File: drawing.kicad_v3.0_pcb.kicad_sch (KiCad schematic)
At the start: 39 parts, among them IC1 DW01A-G, J1 Micro USB Chargeport, J2 Prog headers, J3 128x32 I2C OLED, J4 TP4056, J5 MK-12C02, J6 Conn_01x02, Q1 FS8205, U1 HT7333-SOT89, U2 ESP-12E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

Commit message: Updated charging circuit
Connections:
- net Batt+: now also J6.2 (Pin_2); no longer J6.1 (Pin_1)
- net GND: now also C4.2, IC1.6 (GND), J6.1 (Pin_1), Q1.1 (S1), Q1.3 (S2); no longer J1.4 (ID), Q1.2 (D12_1)
- net at R12.1: now also J4.6 (~{STDBY}); no longer J4.7 (~{CHRG})
- net at IC1.5 (VCC), R14.2: now also C4.1; no longer C4.2
- net at R10.2: now also J4.7 (~{CHRG}); no longer J4.6 (~{STDBY})
- net +5V: no longer names the net of C2.2, D5.2 (A), D6.2 (A), J1.1 (VBUS), J4.4 (VCC4), J4.8 (CE)
- removed net Batt-: C4.1, IC1.6 (GND), J6.2 (Pin_2), Q1.5 (D12_2)
- no-connect marks 19 -> 22
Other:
- moved on the sheet: C1, C2, C3, D5, D6, D7, J1, J2, J3, J4, J5, J6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

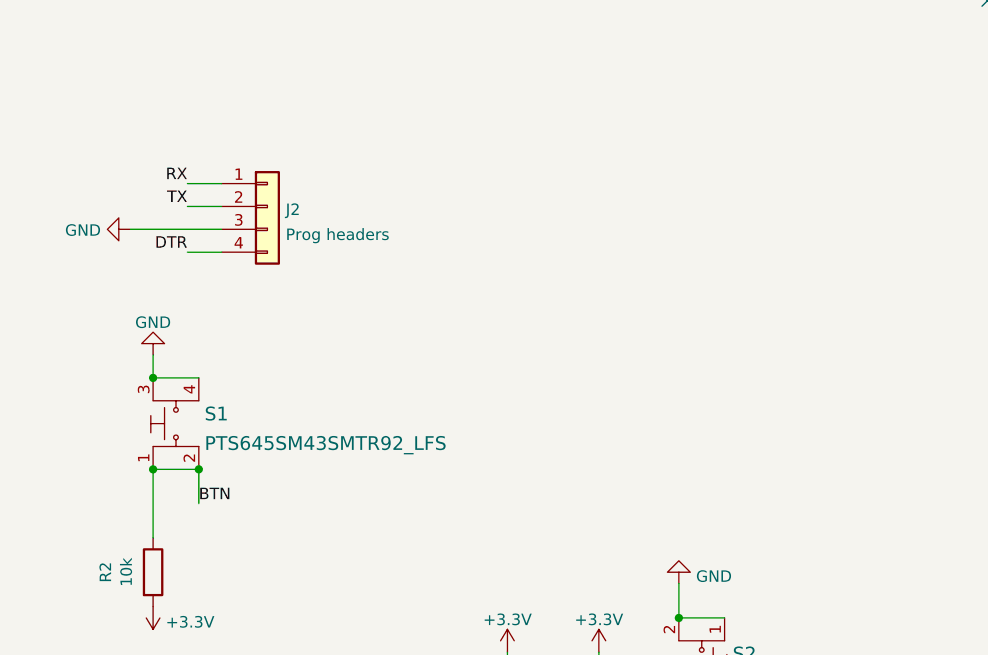
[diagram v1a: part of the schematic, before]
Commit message: Fixed charging circuit in v3.0
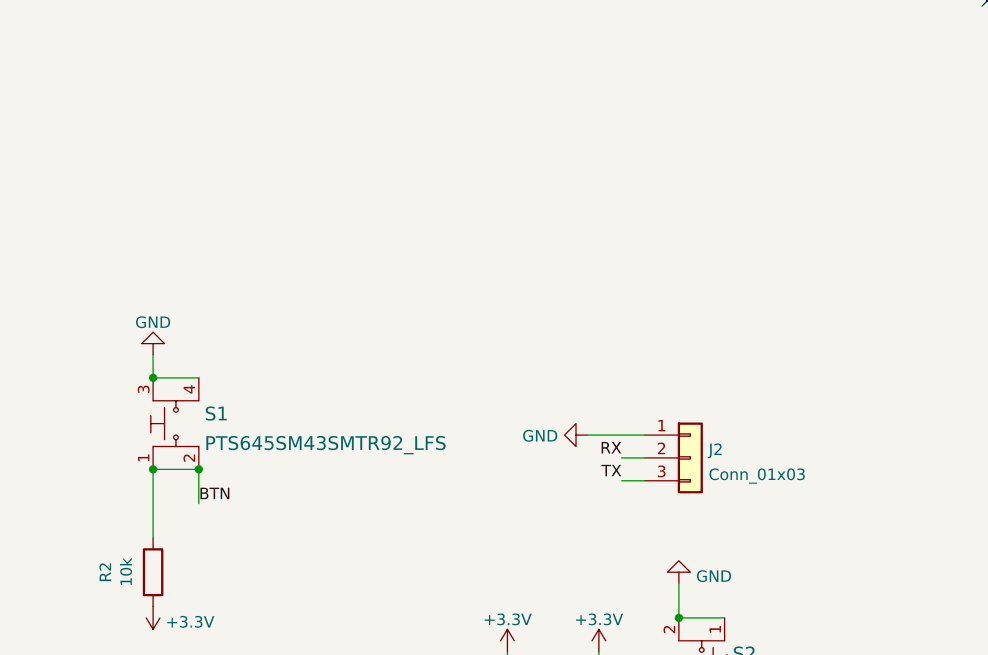
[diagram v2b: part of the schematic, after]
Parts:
- removed J2: Prog headers, Connector_PinSocket_2.54mm:PinSocket_1x04_P2.54mm_Horizontal, symbol Connector_Generic:Conn_01x04
- added J2: Conn_01x03, Connector_PinSocket_2.54mm:PinSocket_1x03_P2.54mm_Horizontal, symbol Connector_Generic:Conn_01x03
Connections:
- net GND: now also J2.1 (Pin_1)
- net RX: now also J2.2 (Pin_2)
- net TX: now also J2.3 (Pin_3)
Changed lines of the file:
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@@
-    (stroke (width 0) (type default) (color 0 0 0 0))
-  )
-  (wire (pts (xy 30.48 82.55) (xy 34.29 82.55))
     (stroke (width 0) (type default) (color 0 0 0 0))
   )
@@
     (stroke (width 0) (type default) (color 0 0 0 0))
   )
-  (wire (pts (xy 24.13 85.09) (xy 34.29 85.09))
-    (stroke (width 0) (type default) (color 0 0 0 0))
-  )
   (wire (pts (xy 231.14 24.13) (xy 238.76 24.13))
     (stroke (width 0) (type default) (color 0 0 0 0))
@@
     (stroke (width 0) (type default) (color 0 0 0 0))
   )
+  (wire (pts (xy 74.93 107.95) (xy 81.28 107.95))
+    (stroke (width 0) (type default) (color 0 0 0 0))
+  )
   (wire (pts (xy 102.87 182.88) (xy 97.79 182.88))
     (stroke (width 0) (type default) (color 0 0 0 0))
@@
     (stroke (width 0) (type default) (color 0 0 0 0))
   )
+  (wire (pts (xy 78.74 113.03) (xy 81.28 113.03))
+    (stroke (width 0) (type default) (color 0 0 0 0))
+  )
   (wire (pts (xy 113.03 160.02) (xy 116.84 160.02))
     (stroke (width 0) (type default) (color 0 0 0 0))
@@
     (stroke (width 0) (type default) (color 0 0 0 0))
   )
-  (wire (pts (xy 30.48 80.01) (xy 34.29 80.01))
-    (stroke (width 0) (type default) (color 0 0 0 0))
-  )
   (wire (pts (xy 130.81 172.72) (xy 130.81 189.23))
     (stroke (width 0) (type default) (color 0 0 0 0))
@@
     (stroke (width 0) (type default) (color 0 0 0 0))
   )
+  (wire (pts (xy 78.74 110.49) (xy 81.28 110.49))
+    (stroke (width 0) (type default) (color 0 0 0 0))
+  )
   (wire (pts (xy 204.47 24.13) (xy 205.74 24.13))
     (stroke (width 0) (type default) (color 0 0 0 0))
@@
   )
   (wire (pts (xy 116.84 186.69) (xy 121.92 186.69))
-    (stroke (width 0) (type default) (color 0 0 0 0))
-  )
-  (wire (pts (xy 30.48 87.63) (xy 34.29 87.63))
     (stroke (width 0) (type default) (color 0 0 0 0))
   )
@@
     (effects (font (size 1.27 1.27)) (justify right bottom))
   )
+  (label "TX" (at 78.74 113.03 180)
+    (effects (font (size 1.27 1.27)) (justify right bottom))
+  )
   (label "SCL" (at 34.29 144.78 0)
     (effects (font (size 1.27 1.27)) (justify left bottom))
@@
     (effects (font (size 1.27 1.27)) (justify right bottom))
   )
-  (label "TX" (at 30.48 82.55 180)
-    (effects (font (size 1.27 1.27)) (justify right bottom))
-  )
   (label "SDA" (at 116.84 160.02 0)
     (effects (font (size 1.27 1.27)) (justify left bottom))
@@
     (effects (font (size 1.27 1.27)) (justify left bottom))
   )
-  (label "RX" (at 30.48 80.01 180)
-    (effects (font (size 1.27 1.27)) (justify right bottom))
-  )
   (label "LC" (at 35.56 46.99 270)
     (effects (font (size 1.27 1.27)) (justify right bottom))
@@
     (effects (font (size 1.27 1.27)) (justify left bottom))
   )
-  (label "DTR" (at 30.48 87.63 180)
+  (label "RX" (at 78.74 110.49 180)
     (effects (font (size 1.27 1.27)) (justify right bottom))
   )
@@
     (pin "1")
   )
+  (symbol (lib_id "power:GND") (at 74.93 107.95 270) (unit 1)
+    (in_bom yes) (on_board yes)
+    (property "Reference" "#PWR02" (id 0) (at 68.58 107.95 0)
+      (effects (font (size 1.27 1.27)) hide)
+    )
+    (property "Value" "GND" (id 1) (at 71.6788 108.077 90)
+      (effects (font (size 1.27 1.27)) (justify right))
+    )
+    (property "Footprint" "" (id 2) (at 74.93 107.95 0)
+      (effects (font (size 1.27 1.27)) hide)
+    )
+    (property "Datasheet" "" (id 3) (at 74.93 107.95 0)
+      (effects (font (size 1.27 1.27)) hide)
+    )
+    (pin "1")
+  )
   (symbol (lib_id "Connector_Generic:Conn_01x04") (at 24.13 147.32 180) (unit 1)
     (in_bom yes) (on_board yes) (fields_autoplaced)
@@
     (pin "1")
     (pin "2")
+  )
+  (symbol (lib_id "Connector_Generic:Conn_01x03") (at 86.36 110.49 0) (unit 1)
+    (in_bom yes) (on_board yes) (fields_autoplaced)
+    (property "Reference" "J2" (id 0) (at 88.392 109.5815 0)
+      (effects (font (size 1.27 1.27)) (justify left))
+    )
+    (property "Value" "Conn_01x03" (id 1) (at 88.392 112.3566 0)
+      (effects (font (size 1.27 1.27)) (justify left))
+    )
+    (property "Footprint" "Connector_PinSocket_2.54mm:PinSocket_1x03_P2.54mm_Horizontal" (id 2) (at 86.36 110.49 0)
+      (effects (font (size 1.27 1.27)) hide)
+    )
+    (property "Datasheet" "~" (id 3) (at 86.36 110.49 0)
+      (effects (font (size 1.27 1.27)) hide)
+    )
+    (pin "1")
+    (pin "2")
+    (pin "3")
   )
   (symbol (lib_id "Device:R") (at 130.81 149.86 270) (unit 1)
@@
     (property "Status" "Active" (id 12) (at 118.11 138.43 0)
       (effects (font (size 1.524 1.524)) (justify left) hide)
-    )
-    (pin "1")
-    (pin "2")
-    (pin "3")
-    (pin "4")
-  )
-  (symbol (lib_id "Connector_Generic:Conn_01x04") (at 39.37 82.55 0) (unit 1)
-    (in_bom yes) (on_board yes) (fields_autoplaced)
-    (property "Reference" "J2" (id 0) (at 41.402 82.9115 0)
-      (effects (font (size 1.27 1.27)) (justify left))
-    )
-    (property "Value" "Prog headers" (id 1) (at 41.402 85.6866 0)
-      (effects (font (size 1.27 1.27)) (justify left))
-    )
-    (property "Footprint" "Connector_PinSocket_2.54mm:PinSocket_1x04_P2.54mm_Horizontal" (id 2) (at 39.37 82.55 0)
-      (effects (font (size 1.27 1.27)) hide)
-    )
-    (property "Datasheet" "~" (id 3) (at 39.37 82.55 0)
-      (effects (font (size 1.27 1.27)) hide)
     )
     (pin "1")
@@
     (pin "2")
   )
-  (symbol (lib_id "power:GND") (at 24.13 85.09 270) (unit 1)
-    (in_bom yes) (on_board yes)
-    (property "Reference" "#PWR02" (id 0) (at 17.78 85.09 0)
-      (effects (font (size 1.27 1.27)) hide)
-    )
-    (property "Value" "GND" (id 1) (at 20.8788 85.217 90)
-      (effects (font (size 1.27 1.27)) (justify right))
-    )
-    (property "Footprint" "" (id 2) (at 24.13 85.09 0)
-      (effects (font (size 1.27 1.27)) hide)
-    )
-    (property "Datasheet" "" (id 3) (at 24.13 85.09 0)
-      (effects (font (size 1.27 1.27)) hide)
-    )
-    (pin "1")
-  )
   (symbol (lib_id "dk_Tactile-Switches:PTS645SM43SMTR92_LFS") (at 29.21 106.68 90) (unit 1)
     (in_bom yes) (on_board yes) (fields_autoplaced)
@@
       (reference "#PWR01") (unit 1) (value "+3.3V") (footprint "")
     )
-    (path "/f3b4c493-5f40-4e19-8b7a-bf81c939d9cc"
+    (path "/44681856-3c12-4f6b-a588-b0d5e9243d70"
       (reference "#PWR02") (unit 1) (value "GND") (footprint "")
     )
@@
       (reference "J1") (unit 1) (value "Micro USB Chargeport") (footprint "digikey-footprints:USB_Micro_B_Female_10118194-0001LF")
     )
-    (path "/9273fd04-97f0-47cf-9769-5fb053b3dd86"
-      (reference "J2") (unit 1) (value "Prog headers") (footprint "Connector_PinSocket_2.54mm:PinSocket_1x04_P2.54mm_Horizontal")
+    (path "/65ba1378-c986-45f1-9d10-63f5630b34c1"
+      (reference "J2") (unit 1) (value "Conn_01x03") (footprint "Connector_PinSocket_2.54mm:PinSocket_1x03_P2.54mm_Horizontal")
     )
     (path "/4eba3540-fbaf-4bf7-8f1f-b9cadb41ae1c"

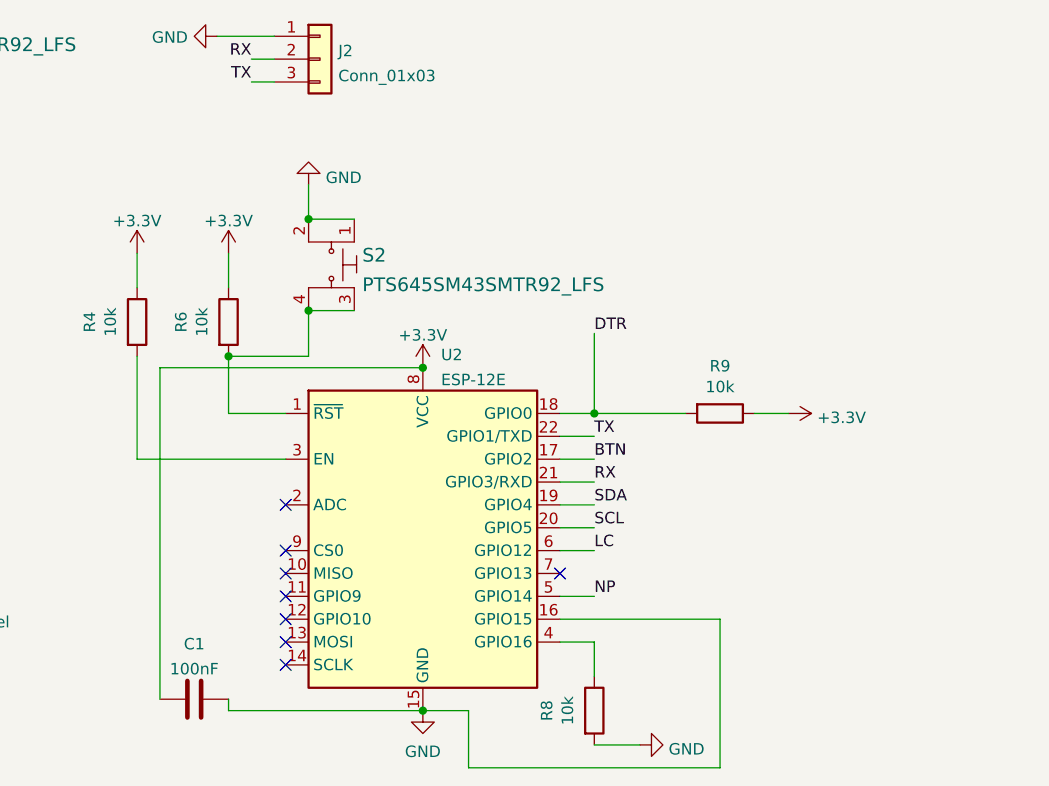
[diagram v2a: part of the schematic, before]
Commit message: Fixed esp8266 programming circuit in v3.0
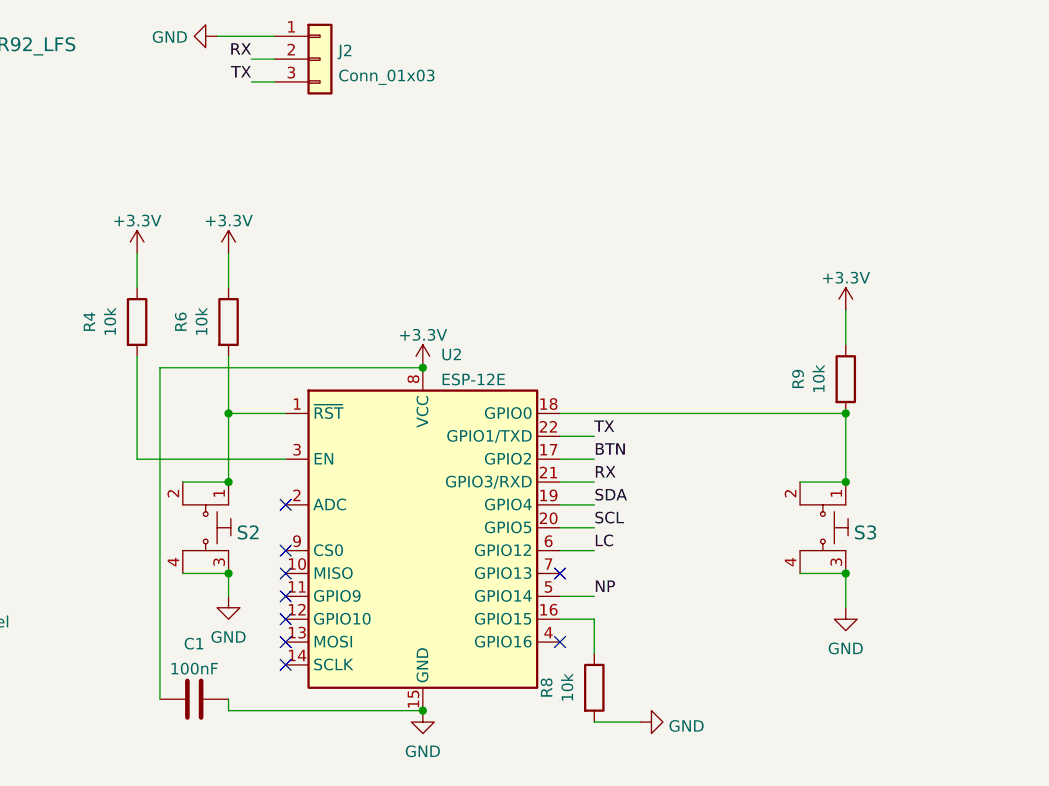
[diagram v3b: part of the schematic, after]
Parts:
- added S3: PTS645SM43SMTR92_LFS, digikey-footprints:Switch_Tactile_SMD_6x6mm_PTS645, symbol dk_Tactile-Switches:PTS645SM43SMTR92_LFS
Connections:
- net GND: now also S2.3, S2.4, S3.3, S3.4; no longer S2.1, S2.2, U2.16 (GPIO15)
- net at R6.2, U2.1 (~{RST}): now also S2.1, S2.2; no longer S2.3, S2.4
- net at R8.1: now also U2.16 (GPIO15); no longer U2.4 (GPIO16)
- net DTR: no longer names the net of R9.2, U2.18 (GPIO0)
- net DTR: now also S3.1, S3.2
- no-connect marks 22 -> 23
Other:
- moved on the sheet: R8, R9, S2
